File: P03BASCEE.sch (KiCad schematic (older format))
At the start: 12 parts

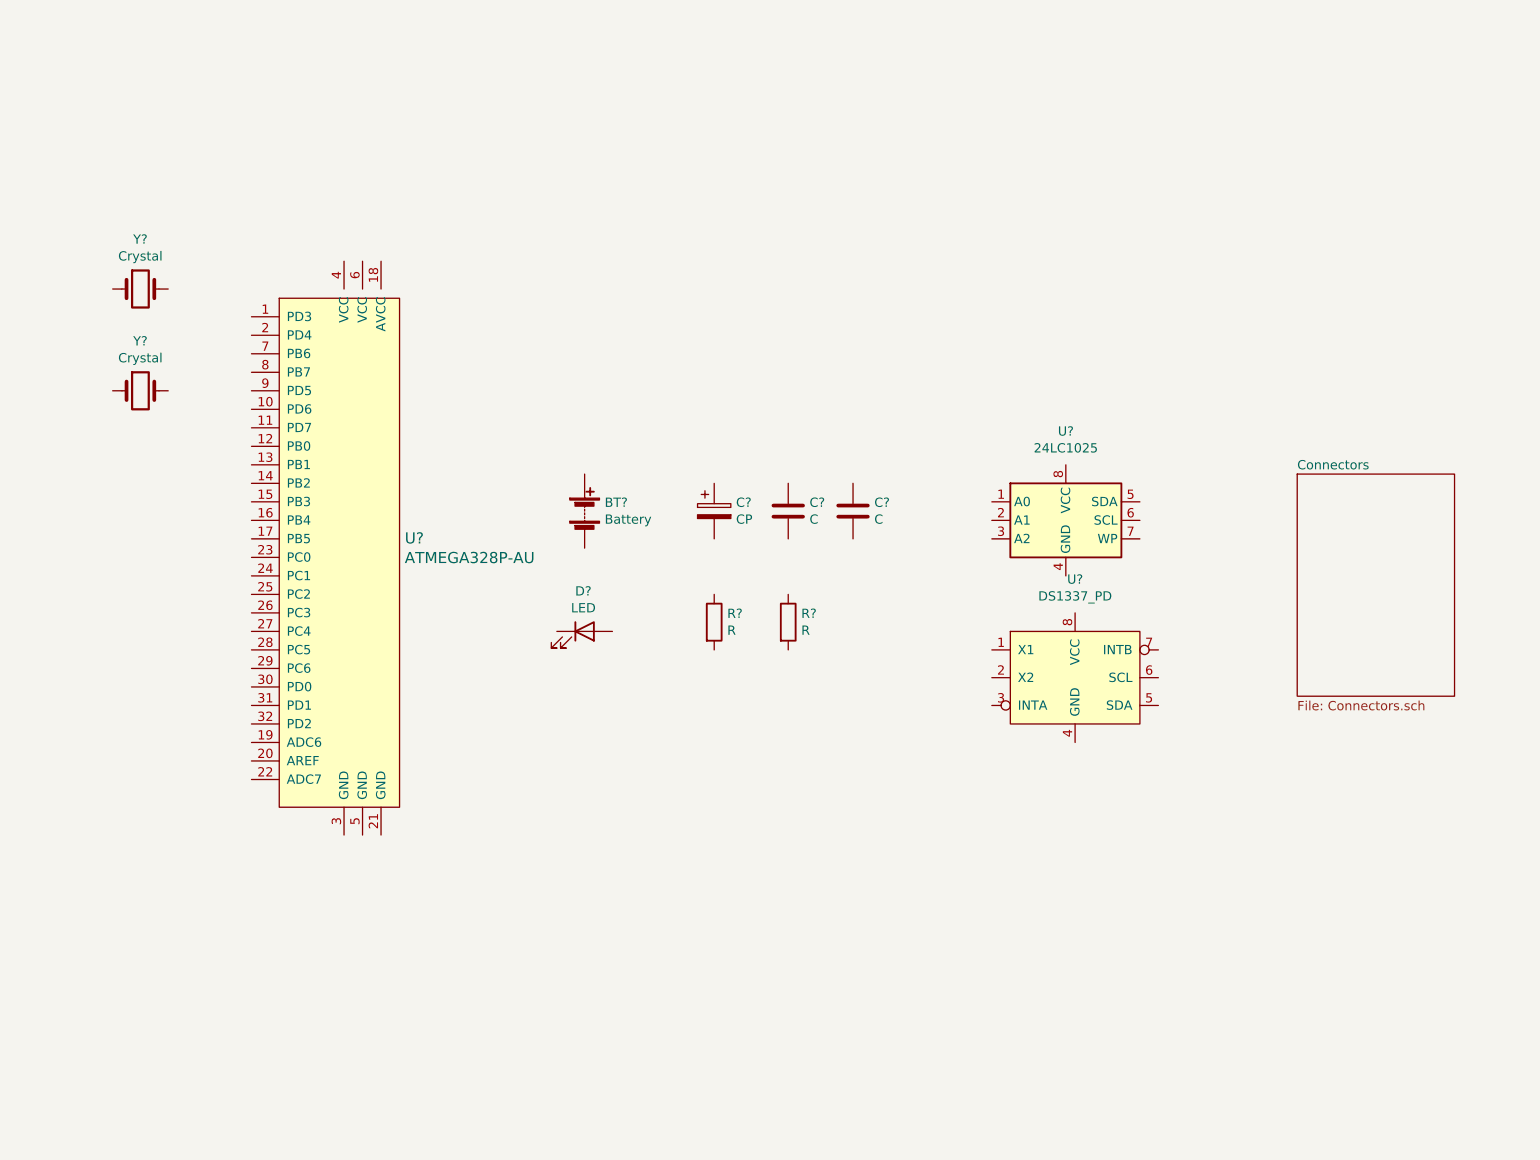
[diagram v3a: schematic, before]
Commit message: Símbolos organizados
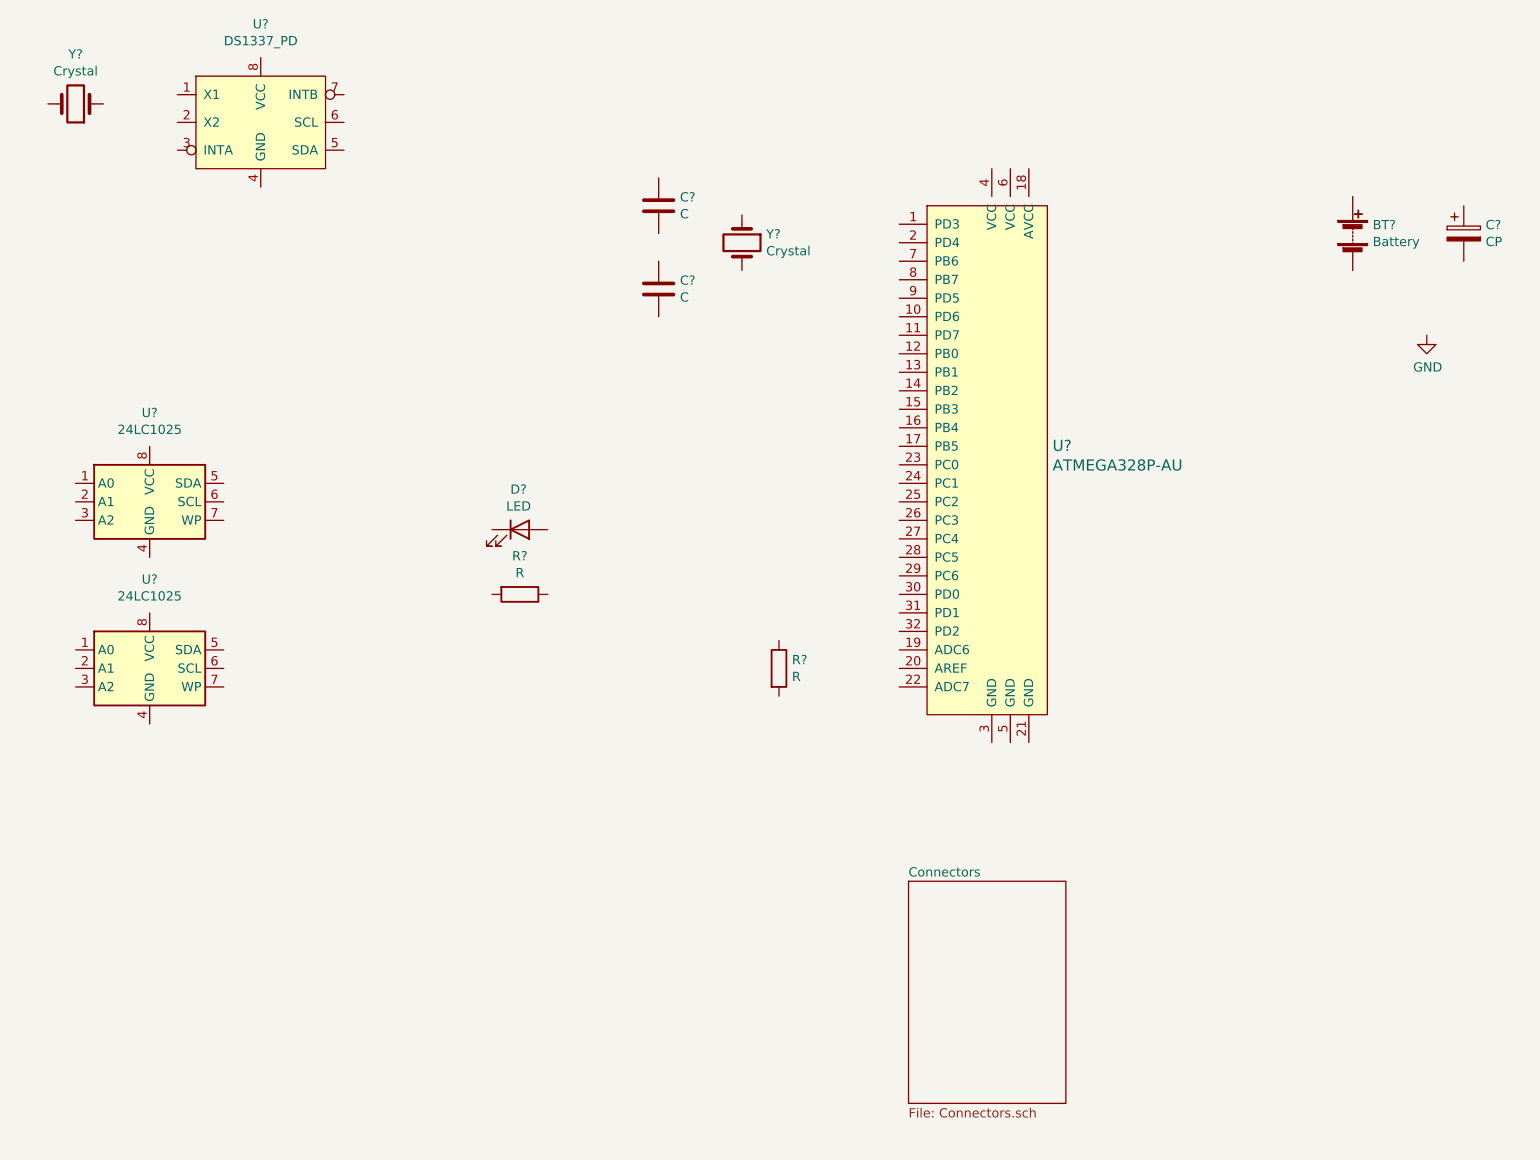
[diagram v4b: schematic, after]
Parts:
- added U?: 24LC1025, symbol Memory_EEPROM:24LC1025
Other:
- moved on the sheet: BT?, C?, D?, R?, U?, Y?
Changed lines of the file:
@@
 L Device:Battery BT?
 U 1 1 5F03198A
-P 4150 4050
-F 0 "BT?" H 4258 4096 50  0000 L CNN
-F 1 "Battery" H 4258 4005 50  0000 L CNN
-F 2 "" V 4150 4110 50  0001 C CNN
-F 3 "~" V 4150 4110 50  0001 C CNN
-	1    4150 4050
+P 8300 2550
+F 0 "BT?" H 8408 2596 50  0000 L CNN
+F 1 "Battery" H 8408 2505 50  0000 L CNN
+F 2 "" V 8300 2610 50  0001 C CNN
+F 3 "~" V 8300 2610 50  0001 C CNN
+	1    8300 2550
 	1    0    0    -1
 $EndComp
@@
 L Device:CP C?
 U 1 1 5F032422
-P 4850 4050
-F 0 "C?" H 4968 4096 50  0000 L CNN
-F 1 "CP" H 4968 4005 50  0000 L CNN
-F 2 "" H 4888 3900 50  0001 C CNN
-F 3 "~" H 4850 4050 50  0001 C CNN
-	1    4850 4050
+P 8900 2550
+F 0 "C?" H 9018 2596 50  0000 L CNN
+F 1 "CP" H 9018 2505 50  0000 L CNN
+F 2 "" H 8938 2400 50  0001 C CNN
+F 3 "~" H 8900 2550 50  0001 C CNN
+	1    8900 2550
 	1    0    0    -1
 $EndComp
@@
 L Device:C C?
 U 1 1 5F032A7C
-P 5250 4050
-F 0 "C?" H 5365 4096 50  0000 L CNN
-F 1 "C" H 5365 4005 50  0000 L CNN
-F 2 "" H 5288 3900 50  0001 C CNN
-F 3 "~" H 5250 4050 50  0001 C CNN
-	1    5250 4050
+P 4550 2850
+F 0 "C?" H 4665 2896 50  0000 L CNN
+F 1 "C" H 4665 2805 50  0000 L CNN
+F 2 "" H 4588 2700 50  0001 C CNN
+F 3 "~" H 4550 2850 50  0001 C CNN
+	1    4550 2850
 	1    0    0    -1
 $EndComp
@@
 L Device:LED D?
 U 1 1 5F032E32
-P 4150 4700
-F 0 "D?" H 4143 4917 50  0000 C CNN
-F 1 "LED" H 4143 4826 50  0000 C CNN
-F 2 "" H 4150 4700 50  0001 C CNN
-F 3 "~" H 4150 4700 50  0001 C CNN
-	1    4150 4700
+P 3800 4150
+F 0 "D?" H 3793 4367 50  0000 C CNN
+F 1 "LED" H 3793 4276 50  0000 C CNN
+F 2 "" H 3800 4150 50  0001 C CNN
+F 3 "~" H 3800 4150 50  0001 C CNN
+	1    3800 4150
 	1    0    0    -1
 $EndComp
@@
 L Device:C C?
 U 1 1 5F0331D2
-P 5600 4050
-F 0 "C?" H 5715 4096 50  0000 L CNN
-F 1 "C" H 5715 4005 50  0000 L CNN
-F 2 "" H 5638 3900 50  0001 C CNN
-F 3 "~" H 5600 4050 50  0001 C CNN
-	1    5600 4050
+P 4550 2400
+F 0 "C?" H 4665 2446 50  0000 L CNN
+F 1 "C" H 4665 2355 50  0000 L CNN
+F 2 "" H 4588 2250 50  0001 C CNN
+F 3 "~" H 4550 2400 50  0001 C CNN
+	1    4550 2400
 	1    0    0    -1
 $EndComp
@@
 L Device:R R?
 U 1 1 5F033AAA
-P 4850 4650
-F 0 "R?" H 4920 4696 50  0000 L CNN
-F 1 "R" H 4920 4605 50  0000 L CNN
-F 2 "" V 4780 4650 50  0001 C CNN
-F 3 "~" H 4850 4650 50  0001 C CNN
-	1    4850 4650
-	1    0    0    -1
+P 3800 4500
+F 0 "R?" V 3593 4500 50  0000 C CNN
+F 1 "R" V 3684 4500 50  0000 C CNN
+F 2 "" V 3730 4500 50  0001 C CNN
+F 3 "~" H 3800 4500 50  0001 C CNN
+	1    3800 4500
+	0    1    1    0
 $EndComp
 $Comp
 L Device:R R?
 U 1 1 5F033ECE
-P 5250 4650
-F 0 "R?" H 5320 4696 50  0000 L CNN
-F 1 "R" H 5320 4605 50  0000 L CNN
-F 2 "" V 5180 4650 50  0001 C CNN
-F 3 "~" H 5250 4650 50  0001 C CNN
-	1    5250 4650
+P 5200 4900
+F 0 "R?" H 5270 4946 50  0000 L CNN
+F 1 "R" H 5270 4855 50  0000 L CNN
+F 2 "" V 5130 4900 50  0001 C CNN
+F 3 "~" H 5200 4900 50  0001 C CNN
+	1    5200 4900
 	1    0    0    -1
 $EndComp
@@
 L Memory_EEPROM:24LC1025 U?
 U 1 1 5F034A3C
-P 6750 4100
-F 0 "U?" H 6750 4581 50  0000 C CNN
-F 1 "24LC1025" H 6750 4490 50  0000 C CNN
-F 2 "" H 6750 4100 50  0001 C CNN
-F 3 "http://ww1.microchip.com/downloads/en/DeviceDoc/21941B.pdf" H 6750 4100 50  0001 C CNN
-	1    6750 4100
+P 1800 4000
+F 0 "U?" H 1800 4481 50  0000 C CNN
+F 1 "24LC1025" H 1800 4390 50  0000 C CNN
+F 2 "" H 1800 4000 50  0001 C CNN
+F 3 "http://ww1.microchip.com/downloads/en/DeviceDoc/21941B.pdf" H 1800 4000 50  0001 C CNN
+	1    1800 4000
 	1    0    0    -1
 $EndComp
 $Sheet
-S 8000 3850 850  1200
+S 5900 6050 850  1200
 U 5F03AF31
 F0 "Connectors" 50
@@
 L dk_Embedded-Microcontrollers:ATMEGA328P-AU U?
 U 1 1 5F040DB0
-P 2850 4300
-F 0 "U?" H 3178 4403 60  0000 L CNN
-F 1 "ATMEGA328P-AU" H 3178 4297 60  0000 L CNN
-F 2 "digikey-footprints:TQFP-32_7x7mm" H 3050 4500 60  0001 L CNN
-F 3 "http://www.microchip.com/mymicrochip/filehandler.aspx?ddocname=en608326" H 3050 4600 60  0001 L CNN
-F 4 "ATMEGA328P-AU-ND" H 3050 4700 60  0001 L CNN "Digi-Key_PN"
-F 5 "ATMEGA328P-AU" H 3050 4800 60  0001 L CNN "MPN"
-F 6 "Integrated Circuits (ICs)" H 3050 4900 60  0001 L CNN "Category"
-F 7 "Embedded - Microcontrollers" H 3050 5000 60  0001 L CNN "Family"
-F 8 "http://www.microchip.com/mymicrochip/filehandler.aspx?ddocname=en608326" H 3050 5100 60  0001 L CNN "DK_Datasheet_Link"
-F 9 "/product-detail/en/microchip-technology/ATMEGA328P-AU/ATMEGA328P-AU-ND/1832260" H 3050 5200 60  0001 L CNN "DK_Detail_Page"
-F 10 "IC MCU 8BIT 32KB FLASH 32TQFP" H 3050 5300 60  0001 L CNN "Description"
-F 11 "Microchip Technology" H 3050 5400 60  0001 L CNN "Manufacturer"
-F 12 "Active" H 3050 5500 60  0001 L CNN "Status"
-	1    2850 4300
+P 6350 3800
+F 0 "U?" H 6678 3903 60  0000 L CNN
+F 1 "ATMEGA328P-AU" H 6678 3797 60  0000 L CNN
+F 2 "digikey-footprints:TQFP-32_7x7mm" H 6550 4000 60  0001 L CNN
+F 3 "http://www.microchip.com/mymicrochip/filehandler.aspx?ddocname=en608326" H 6550 4100 60  0001 L CNN
+F 4 "ATMEGA328P-AU-ND" H 6550 4200 60  0001 L CNN "Digi-Key_PN"
+F 5 "ATMEGA328P-AU" H 6550 4300 60  0001 L CNN "MPN"
+F 6 "Integrated Circuits (ICs)" H 6550 4400 60  0001 L CNN "Category"
+F 7 "Embedded - Microcontrollers" H 6550 4500 60  0001 L CNN "Family"
+F 8 "http://www.microchip.com/mymicrochip/filehandler.aspx?ddocname=en608326" H 6550 4600 60  0001 L CNN "DK_Datasheet_Link"
+F 9 "/product-detail/en/microchip-technology/ATMEGA328P-AU/ATMEGA328P-AU-ND/1832260" H 6550 4700 60  0001 L CNN "DK_Detail_Page"
+F 10 "IC MCU 8BIT 32KB FLASH 32TQFP" H 6550 4800 60  0001 L CNN "Description"
+F 11 "Microchip Technology" H 6550 4900 60  0001 L CNN "Manufacturer"
+F 12 "Active" H 6550 5000 60  0001 L CNN "Status"
+	1    6350 3800
 	1    0    0    -1
 $EndComp
@@
 L DS1337:DS1337_PD U?
 U 1 1 5F04ABB9
-P 6800 4950
-F 0 "U?" H 6800 5481 50  0000 C CNN
-F 1 "DS1337_PD" H 6800 5390 50  0000 C CNN
-F 2 "" H 6800 5350 50  0001 C CNN
-F 3 "https://datasheets.maximintegrated.com/en/ds/DS1337-DS1337C.pdf" H 6800 5350 50  0001 C CNN
-	1    6800 4950
+P 2400 1950
+F 0 "U?" H 2400 2481 50  0000 C CNN
+F 1 "DS1337_PD" H 2400 2390 50  0000 C CNN
+F 2 "" H 2400 2350 50  0001 C CNN
+F 3 "https://datasheets.maximintegrated.com/en/ds/DS1337-DS1337C.pdf" H 2400 2350 50  0001 C CNN
+	1    2400 1950
 	1    0    0    -1
 $EndComp
@@
 L Device:Crystal Y?
 U 1 1 5F04BC1B
-P 1750 2850
-F 0 "Y?" H 1750 3118 50  0000 C CNN
-F 1 "Crystal" H 1750 3027 50  0000 C CNN
-F 2 "" H 1750 2850 50  0001 C CNN
-F 3 "~" H 1750 2850 50  0001 C CNN
-	1    1750 2850
-	1    0    0    -1
+P 5000 2600
+F 0 "Y?" V 4954 2731 50  0000 L CNN
+F 1 "Crystal" V 5045 2731 50  0000 L CNN
+F 2 "" H 5000 2600 50  0001 C CNN
+F 3 "~" H 5000 2600 50  0001 C CNN
+	1    5000 2600
+	0    1    1    0
 $EndComp
 $Comp
 L Device:Crystal Y?
 U 1 1 5F04CD00
-P 1750 3400
-F 0 "Y?" H 1750 3668 50  0000 C CNN
-F 1 "Crystal" H 1750 3577 50  0000 C CNN
-F 2 "" H 1750 3400 50  0001 C CNN
-F 3 "~" H 1750 3400 50  0001 C CNN
-	1    1750 3400
+P 1400 1850
+F 0 "Y?" H 1400 1582 50  0000 C CNN
+F 1 "Crystal" H 1400 1673 50  0000 C CNN
+F 2 "" H 1400 1850 50  0001 C CNN
+F 3 "~" H 1400 1850 50  0001 C CNN
+	1    1400 1850
+	-1   0    0    1
+$EndComp
+$Comp
+L Memory_EEPROM:24LC1025 U?
+U 1 1 5F05520E
+P 1800 4900
+F 0 "U?" H 1800 5381 50  0000 C CNN
+F 1 "24LC1025" H 1800 5290 50  0000 C CNN
+F 2 "" H 1800 4900 50  0001 C CNN
+F 3 "http://ww1.microchip.com/downloads/en/DeviceDoc/21941B.pdf" H 1800 4900 50  0001 C CNN
+	1    1800 4900
 	1    0    0    -1
 $EndComp
+$Comp
+L power:GND #PWR?
+U 1 1 5F0655B3
+P 8700 3100
+F 0 "#PWR?" H 8700 2850 50  0001 C CNN
+F 1 "GND" H 8705 2927 50  0000 C CNN
+F 2 "" H 8700 3100 50  0001 C CNN
+F 3 "" H 8700 3100 50  0001 C CNN
+	1    8700 3100
+	1    0    0    -1
+$EndComp

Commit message: Símbolos anotados
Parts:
- gave numbers to parts that had none: 13
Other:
- moved on the sheet: D1
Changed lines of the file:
@@
 $EndDescr
 $Comp
-L Device:Battery BT?
+L Device:Battery BT1
 U 1 1 5F03198A
 P 8300 2550
-F 0 "BT?" H 8408 2596 50  0000 L CNN
+F 0 "BT1" H 8408 2596 50  0000 L CNN
 F 1 "Battery" H 8408 2505 50  0000 L CNN
 F 2 "" V 8300 2610 50  0001 C CNN
@@
 $EndComp
 $Comp
-L Device:CP C?
+L Device:CP C3
 U 1 1 5F032422
 P 8900 2550
-F 0 "C?" H 9018 2596 50  0000 L CNN
+F 0 "C3" H 9018 2596 50  0000 L CNN
 F 1 "CP" H 9018 2505 50  0000 L CNN
 F 2 "" H 8938 2400 50  0001 C CNN
@@
 $EndComp
 $Comp
-L Device:C C?
+L Device:C C2
 U 1 1 5F032A7C
 P 4550 2850
-F 0 "C?" H 4665 2896 50  0000 L CNN
+F 0 "C2" H 4665 2896 50  0000 L CNN
 F 1 "C" H 4665 2805 50  0000 L CNN
 F 2 "" H 4588 2700 50  0001 C CNN
@@
 $EndComp
 $Comp
-L Device:LED D?
+L Device:LED D1
 U 1 1 5F032E32
-P 3800 4150
-F 0 "D?" H 3793 4367 50  0000 C CNN
-F 1 "LED" H 3793 4276 50  0000 C CNN
-F 2 "" H 3800 4150 50  0001 C CNN
-F 3 "~" H 3800 4150 50  0001 C CNN
-	1    3800 4150
+P 3850 3800
+F 0 "D1" H 3843 4017 50  0000 C CNN
+F 1 "LED" H 3843 3926 50  0000 C CNN
+F 2 "" H 3850 3800 50  0001 C CNN
+F 3 "~" H 3850 3800 50  0001 C CNN
+	1    3850 3800
 	1    0    0    -1
 $EndComp
 $Comp
-L Device:C C?
+L Device:C C1
 U 1 1 5F0331D2
 P 4550 2400
-F 0 "C?" H 4665 2446 50  0000 L CNN
+F 0 "C1" H 4665 2446 50  0000 L CNN
 F 1 "C" H 4665 2355 50  0000 L CNN
 F 2 "" H 4588 2250 50  0001 C CNN
@@
 $EndComp
 $Comp
-L Device:R R?
+L Device:R R1
 U 1 1 5F033AAA
 P 3800 4500
-F 0 "R?" V 3593 4500 50  0000 C CNN
+F 0 "R1" V 3593 4500 50  0000 C CNN
 F 1 "R" V 3684 4500 50  0000 C CNN
 F 2 "" V 3730 4500 50  0001 C CNN
@@
 $EndComp
 $Comp
-L Device:R R?
+L Device:R R2
 U 1 1 5F033ECE
 P 5200 4900
-F 0 "R?" H 5270 4946 50  0000 L CNN
+F 0 "R2" H 5270 4946 50  0000 L CNN
 F 1 "R" H 5270 4855 50  0000 L CNN
 F 2 "" V 5130 4900 50  0001 C CNN
@@
 $EndComp
 $Comp
-L Memory_EEPROM:24LC1025 U?
+L Memory_EEPROM:24LC1025 U1
 U 1 1 5F034A3C
 P 1800 4000
-F 0 "U?" H 1800 4481 50  0000 C CNN
+F 0 "U1" H 1800 4481 50  0000 C CNN
 F 1 "24LC1025" H 1800 4390 50  0000 C CNN
 F 2 "" H 1800 4000 50  0001 C CNN
@@
 $EndSheet
 $Comp
-L dk_Embedded-Microcontrollers:ATMEGA328P-AU U?
+L dk_Embedded-Microcontrollers:ATMEGA328P-AU U4
 U 1 1 5F040DB0
 P 6350 3800
-F 0 "U?" H 6678 3903 60  0000 L CNN
+F 0 "U4" H 6678 3903 60  0000 L CNN
 F 1 "ATMEGA328P-AU" H 6678 3797 60  0000 L CNN
 F 2 "digikey-footprints:TQFP-32_7x7mm" H 6550 4000 60  0001 L CNN
@@
 $EndComp
 $Comp
-L DS1337:DS1337_PD U?
+L DS1337:DS1337_PD U3
 U 1 1 5F04ABB9
 P 2400 1950
-F 0 "U?" H 2400 2481 50  0000 C CNN
+F 0 "U3" H 2400 2481 50  0000 C CNN
 F 1 "DS1337_PD" H 2400 2390 50  0000 C CNN
 F 2 "" H 2400 2350 50  0001 C CNN
@@
 $EndComp
 $Comp
-L Device:Crystal Y?
+L Device:Crystal Y2
 U 1 1 5F04BC1B
 P 5000 2600
-F 0 "Y?" V 4954 2731 50  0000 L CNN
+F 0 "Y2" V 4954 2731 50  0000 L CNN
 F 1 "Crystal" V 5045 2731 50  0000 L CNN
 F 2 "" H 5000 2600 50  0001 C CNN
@@
 $EndComp
 $Comp
-L Device:Crystal Y?
+L Device:Crystal Y1
 U 1 1 5F04CD00
 P 1400 1850
-F 0 "Y?" H 1400 1582 50  0000 C CNN
+F 0 "Y1" H 1400 1582 50  0000 C CNN
 F 1 "Crystal" H 1400 1673 50  0000 C CNN
 F 2 "" H 1400 1850 50  0001 C CNN
@@
 $EndComp
 $Comp
-L Memory_EEPROM:24LC1025 U?
+L Memory_EEPROM:24LC1025 U2
 U 1 1 5F05520E
 P 1800 4900
-F 0 "U?" H 1800 5381 50  0000 C CNN
+F 0 "U2" H 1800 5381 50  0000 C CNN
 F 1 "24LC1025" H 1800 5290 50  0000 C CNN
 F 2 "" H 1800 4900 50  0001 C CNN
@@
 $EndComp
 $Comp
-L power:GND #PWR?
+L power:GND #PWR01
 U 1 1 5F0655B3
 P 8700 3100
-F 0 "#PWR?" H 8700 2850 50  0001 C CNN
+F 0 "#PWR01" H 8700 2850 50  0001 C CNN
 F 1 "GND" H 8705 2927 50  0000 C CNN
 F 2 "" H 8700 3100 50  0001 C CNN
